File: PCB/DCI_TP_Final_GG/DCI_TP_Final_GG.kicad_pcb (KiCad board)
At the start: 2 copper layers, 42 x 90 mm, 69 parts, among them J201 DRIVER A OUT, J301 DRIVER B OUT, J401 IN - Driver A, J402 IN - Driver B, J403 Vin, J404 Vout, U201 A3967, U301 A3967, U401 LM317

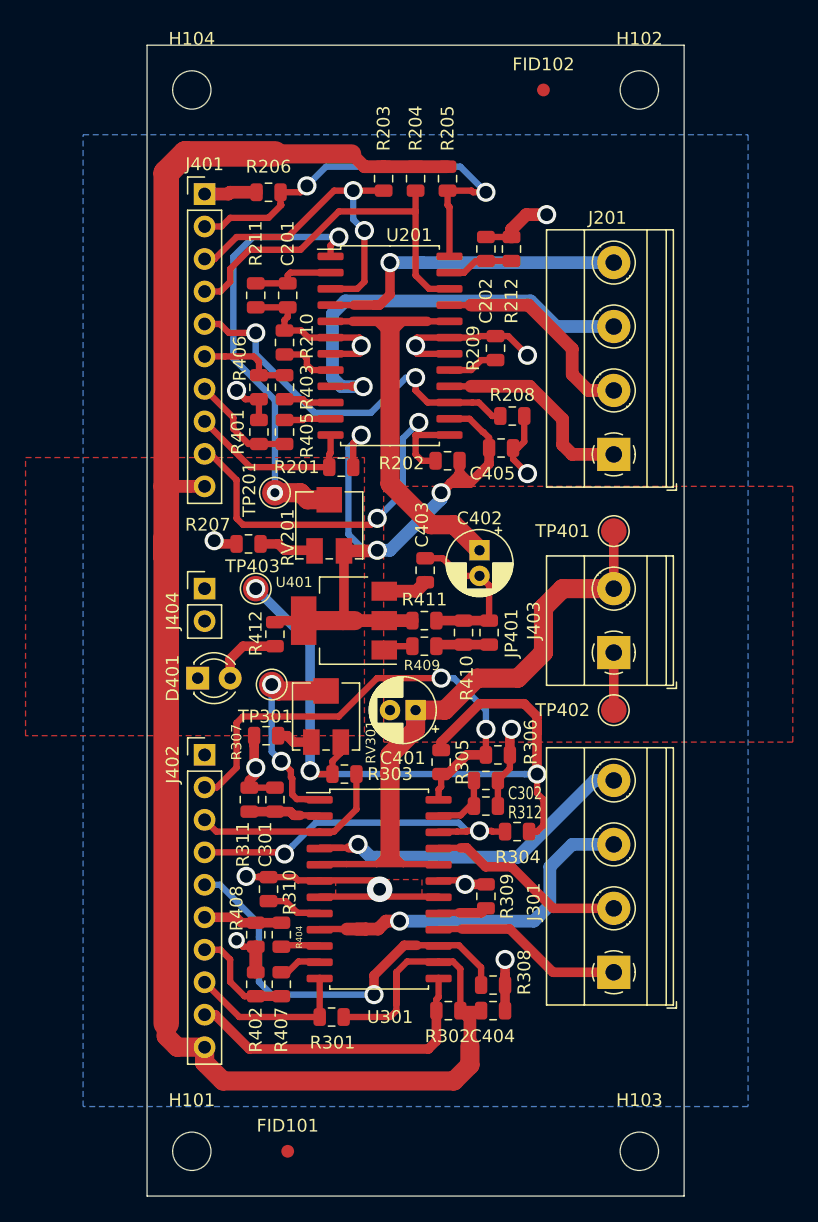
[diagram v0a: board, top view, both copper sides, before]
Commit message: Agrego 3D de borneras
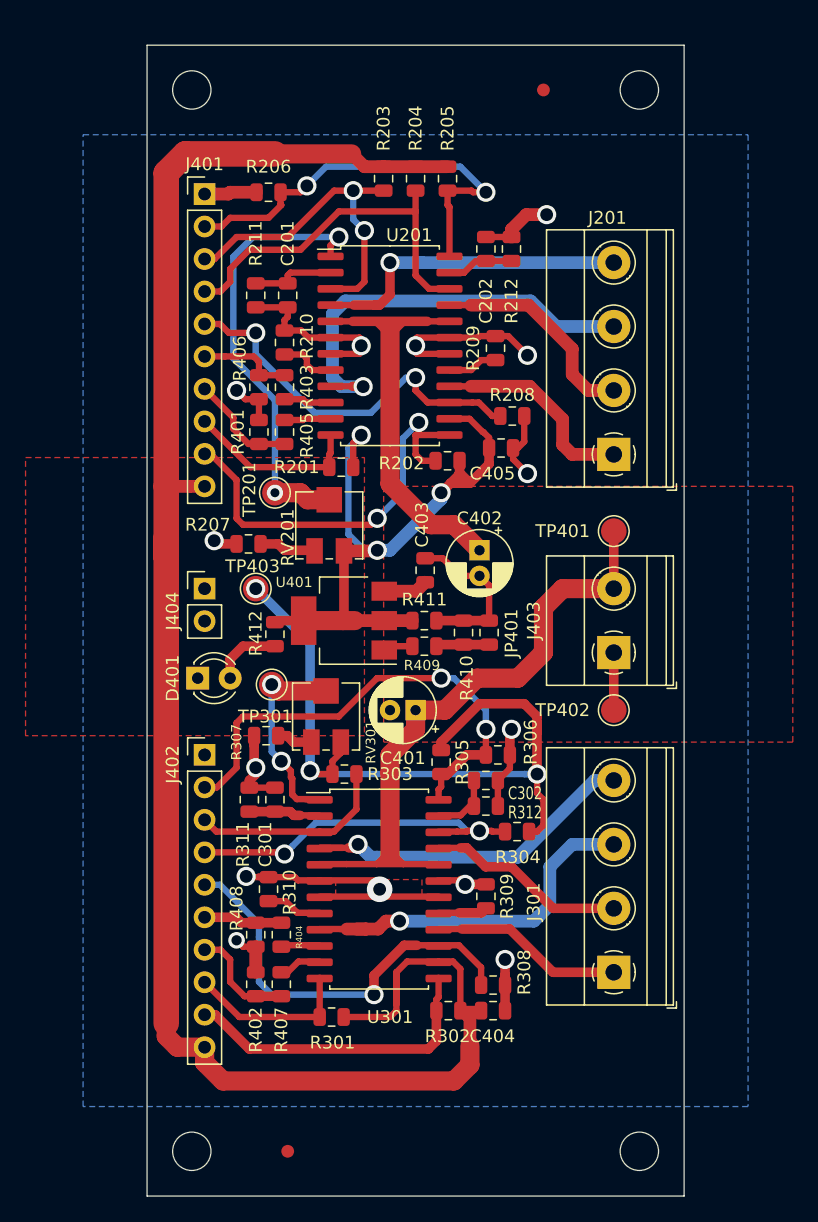
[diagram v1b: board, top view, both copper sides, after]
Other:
- board text added: "Grilla componentes: 5mm, 2,5mm, 1mm y 0.5mm(para ajuste fino en el control de clearance) Grilla pistas: 1mm, 0.5mm, 0.25mm y 0.1 (para ajuste fino) Vias: 1.3mm ,1.5mm y 2mm (Limite Mayer=1.27) Pistas: 0.5mm, 0.75mm, 1mm, 1.5mm, 2mm (limite Mayer = 0.3mm) Clearance > 0.3 mm (Limite Mayer=0.3mm) PCB FR4 - sustratos 1.6mm de espesor Cobre 1 Oz Terminacion HASL"
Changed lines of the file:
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@@
   (general
     (thickness 1.6)
-    (drawings 4)
+    (drawings 7)
     (tracks 558)
     (zones 0)
@@
     (0 F.Cu signal)
     (31 B.Cu signal)
-    (32 B.Adhes user hide)
-    (33 F.Adhes user hide)
-    (34 B.Paste user hide)
-    (35 F.Paste user hide)
+    (32 B.Adhes user)
+    (33 F.Adhes user)
+    (34 B.Paste user)
+    (35 F.Paste user)
     (36 B.SilkS user)
     (37 F.SilkS user)
     (38 B.Mask user)
     (39 F.Mask user)
-    (40 Dwgs.User user hide)
+    (40 Dwgs.User user)
     (41 Cmts.User user)
-    (42 Eco1.User user hide)
-    (43 Eco2.User user hide)
+    (42 Eco1.User user)
+    (43 Eco2.User user)
     (44 Edge.Cuts user)
     (45 Margin user)
-    (46 B.CrtYd user hide)
+    (46 B.CrtYd user)
     (47 F.CrtYd user)
-    (48 B.Fab user hide)
-    (49 F.Fab user hide)
+    (48 B.Fab user)
+    (49 F.Fab user)
   )
   (setup
-    (last_trace_width 0.75)
+    (last_trace_width 0.3)
     (user_trace_width 0.3)
     (user_trace_width 0.5)
@@
       (rotate (xyz 0 0 0))
     )
+    (model "${KIPRJMOD}/MKDS series connectors/3d_conn_mkds/walter/conn_mkds/mkds_1,5-4.wrl"
+      (offset (xyz 7.5 0 0))
+      (scale (xyz 1 1 1))
+      (rotate (xyz 0 0 0))
+    )
   )
   (module Package_SO:SOIC-24W_7.5x15.4mm_P1.27mm (layer F.Cu)
@@
       (net 1 GND))
     (model ${KISYS3DMOD}/TerminalBlock_Phoenix.3dshapes/TerminalBlock_Phoenix_MKDS-1,5-2_1x02_P5.00mm_Horizontal.wrl
-      (at (xyz 0 0 0))
+      (offset (xyz 0.5 0 0))
+      (scale (xyz 1 1 1))
+      (rotate (xyz 0 0 0))
+    )
+    (model "${KIPRJMOD}/MKDS series connectors/3d_conn_mkds/walter/conn_mkds/mkds_1,5-2.wrl"
+      (offset (xyz 2.5 0 0))
       (scale (xyz 1 1 1))
       (rotate (xyz 0 0 0))
@@
       (effects (font (size 1 1) (thickness 0.15)))
     )
-    (fp_text value "VRef A" (at 0 2.05 90) (layer F.Fab)
+    (fp_text value "VRef A" (at -0.5 2.25 90) (layer F.Fab)
       (effects (font (size 1 1) (thickness 0.15)))
     )
@@
       (effects (font (size 1 1) (thickness 0.15)))
     )
-    (fp_text value 1K (at 0 1.65 90) (layer F.Fab)
+    (fp_text value 1K (at 0 3.5 90) (layer F.Fab)
       (effects (font (size 1 1) (thickness 0.15)))
     )
@@
       (effects (font (size 1 1) (thickness 0.15)))
     )
-    (fp_text value 10K (at 0 1.65 90) (layer F.Fab)
+    (fp_text value 10K (at -0.0625 3.5 90) (layer F.Fab)
       (effects (font (size 1 1) (thickness 0.15)))
     )
@@
       (effects (font (size 1 1) (thickness 0.15)))
     )
-    (fp_text value 6.8K (at 0 1.65) (layer F.Fab)
+    (fp_text value 6.8K (at 1.5625 2.5) (layer F.Fab)
       (effects (font (size 1 1) (thickness 0.15)))
     )
@@
       (effects (font (size 1 1) (thickness 0.15)))
     )
-    (fp_text value Vout (at 0 4.87) (layer F.Fab)
+    (fp_text value Vout (at -2 2 90) (layer F.Fab)
       (effects (font (size 1 1) (thickness 0.15)))
     )
@@
       (net 12 "/Driver A/DA-O1A"))
     (model ${KISYS3DMOD}/TerminalBlock_Phoenix.3dshapes/TerminalBlock_Phoenix_MKDS-1,5-4_1x04_P5.00mm_Horizontal.wrl
-      (at (xyz 0 0 0))
+      (offset (xyz 0 -7.5 0))
+      (scale (xyz 1 1 1))
+      (rotate (xyz 0 0 0))
+    )
+    (model "${KIPRJMOD}/MKDS series connectors/3d_conn_mkds/walter/conn_mkds/mkds_1,5-4.wrl"
+      (offset (xyz 7.5 0 0))
       (scale (xyz 1 1 1))
       (rotate (xyz 0 0 0))
@@
     (tags "mounting hole 3mm no annular")
     (attr virtual)
-    (fp_text reference H104 (at 0 -4) (layer F.SilkS)
+    (fp_text reference H104 (at 0 4.5) (layer F.SilkS) hide
       (effects (font (size 1 1) (thickness 0.15)))
     )
@@
     (tags "mounting hole 3mm no annular")
     (attr virtual)
-    (fp_text reference H103 (at 0 -4) (layer F.SilkS)
+    (fp_text reference H103 (at 0 -4) (layer F.SilkS) hide
       (effects (font (size 1 1) (thickness 0.15)))
     )
@@
     (tags "mounting hole 3mm no annular")
     (attr virtual)
-    (fp_text reference H102 (at 0 -4) (layer F.SilkS)
+    (fp_text reference H102 (at 0 4.5) (layer F.SilkS) hide
       (effects (font (size 1 1) (thickness 0.15)))
     )
@@
     (tags "mounting hole 3mm no annular")
     (attr virtual)
-    (fp_text reference H101 (at 0 -4) (layer F.SilkS)
+    (fp_text reference H101 (at 0 -4) (layer F.SilkS) hide
       (effects (font (size 1 1) (thickness 0.15)))
     )
@@
     (tags fiducial)
     (attr smd)
-    (fp_text reference FID102 (at 0 -2) (layer F.SilkS)
+    (fp_text reference FID102 (at 0 -2) (layer F.SilkS) hide
       (effects (font (size 1 1) (thickness 0.15)))
     )
@@
     (tags fiducial)
     (attr smd)
-    (fp_text reference FID101 (at 0 -2) (layer F.SilkS)
+    (fp_text reference FID101 (at 0 -2) (layer F.SilkS) hide
       (effects (font (size 1 1) (thickness 0.15)))
     )
@@
       (effects (font (size 1 1) (thickness 0.15)))
     )
-    (fp_text value LED (at 1.27 2.96) (layer F.Fab)
+    (fp_text value LED (at -0.96 0.5 90) (layer F.Fab)
       (effects (font (size 1 1) (thickness 0.15)))
     )
@@
     )
   )
+  (dimension 90 (width 0.15) (layer F.Fab)
+    (gr_text "90,000 mm" (at 96.7 95.5 270) (layer F.Fab)
+      (effects (font (size 1 1) (thickness 0.15)))
+    )
+    (feature1 (pts (xy 106.5 140.5) (xy 97.413579 140.5)))
+    (feature2 (pts (xy 106.5 50.5) (xy 97.413579 50.5)))
+    (crossbar (pts (xy 98 50.5) (xy 98 140.5)))
+    (arrow1a (pts (xy 98 140.5) (xy 97.413579 139.373496)))
+    (arrow1b (pts (xy 98 140.5) (xy 98.586421 139.373496)))
+    (arrow2a (pts (xy 98 50.5) (xy 97.413579 51.626504)))
+    (arrow2b (pts (xy 98 50.5) (xy 98.586421 51.626504)))
+  )
+  (dimension 42 (width 0.15) (layer F.Fab)
+    (gr_text "42,000 mm" (at 127.5 43.2) (layer F.Fab)
+      (effects (font (size 1 1) (thickness 0.15)))
+    )
+    (feature1 (pts (xy 148.5 50.5) (xy 148.5 43.913579)))
+    (feature2 (pts (xy 106.5 50.5) (xy 106.5 43.913579)))
+    (crossbar (pts (xy 106.5 44.5) (xy 148.5 44.5)))
+    (arrow1a (pts (xy 148.5 44.5) (xy 147.373496 45.086421)))
+    (arrow1b (pts (xy 148.5 44.5) (xy 147.373496 43.913579)))
+    (arrow2a (pts (xy 106.5 44.5) (xy 107.626504 45.086421)))
+    (arrow2b (pts (xy 106.5 44.5) (xy 107.626504 43.913579)))
+  )
+  (gr_text "Grilla componentes: 5mm, 2,5mm,\n 1mm y 0.5mm(para ajuste fino en\nel control de clearance)\n\nGrilla pistas: 1mm, 0.5mm, 0.25mm \ny 0.1 (para ajuste fino)\n\nVias: 1.3mm ,1.5mm y 2mm (Limite Mayer=1.27)\n\nPistas: 0.5mm, 0.75mm, 1mm, 1.5mm, 2mm\n(limite Mayer = 0.3mm)\n\nClearance > 0.3 mm  (Limite Mayer=0.3mm)\n\nPCB\nFR4 - sustratos 1.6mm de espesor\nCobre 1 Oz\nTerminacion HASL\n\n" (at 175.5 87) (layer Dwgs.User)
+    (effects (font (size 1 1) (thickness 0.15)) (justify left))
+  )
   (gr_line (start 106.5 50.5) (end 106.5 140.5) (layer Edge.Cuts) (width 0.05))

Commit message: Agrego codigos de catalogo
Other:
- board text added: "Gonzalo Gontad DCI - CESE - FIUBA"
- board text added: "Industria Argentina"
- board text added: "V1019"
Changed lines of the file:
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@@
-(kicad_pcb (version 20171130) (host pcbnew "(5.1.4)-1")
+(kicad_pcb (version 20171130) (host pcbnew 5.1.4-e60b266~84~ubuntu18.04.1)
   (general
     (thickness 1.6)
-    (drawings 7)
+    (drawings 10)
     (tracks 558)
     (zones 0)
@@
   )
   (page A4)
+  (title_block
+    (title "Replica Dual EasyDriver v4.5")
+    (date 2019-10-17)
+    (rev "Matias Brignone")
+    (company "Gonzalo Gontad - CESE-FIUBA")
+  )
   (layers
     (0 F.Cu signal)
     (31 B.Cu signal)
-    (32 B.Adhes user)
-    (33 F.Adhes user)
-    (34 B.Paste user)
-    (35 F.Paste user)
-    (36 B.SilkS user)
+    (32 B.Adhes user hide)
+    (33 F.Adhes user hide)
+    (34 B.Paste user hide)
+    (35 F.Paste user hide)
+    (36 B.SilkS user hide)
     (37 F.SilkS user)
-    (38 B.Mask user)
+    (38 B.Mask user hide)
     (39 F.Mask user)
     (40 Dwgs.User user)
-    (41 Cmts.User user)
-    (42 Eco1.User user)
-    (43 Eco2.User user)
+    (41 Cmts.User user hide)
+    (42 Eco1.User user hide)
+    (43 Eco2.User user hide)
     (44 Edge.Cuts user)
     (45 Margin user)
-    (46 B.CrtYd user)
+    (46 B.CrtYd user hide)
     (47 F.CrtYd user)
-    (48 B.Fab user)
-    (49 F.Fab user)
+    (48 B.Fab user hide)
+    (49 F.Fab user hide)
   )
   (setup
@@
       (rotate (xyz 0 0 0))
     )
+    (model ${KIPRJMOD}/Potentiometer_SMD.3dshapes/Potentiometer_Bourns_3314J_Vertical.step
+      (at (xyz 0 0 0))
+      (scale (xyz 1 1 1))
+      (rotate (xyz 0 0 90))
+    )
   )
   (module Potentiometer_SMD:Potentiometer_Vishay_TS53YJ_Vertical (layer F.Cu)
@@
       (at (xyz 0 0 0))
       (scale (xyz 1 1 1))
-      (rotate (xyz 0 0 0))
+      (rotate (xyz 0 0 90))
+    )
+    (model ${KIPRJMOD}/Potentiometer_SMD.3dshapes/Potentiometer_Bourns_3314J_Vertical.step
+      (at (xyz 0 0 0))
+      (scale (xyz 1 1 1))
+      (rotate (xyz 0 0 90))
     )
   )
@@
     )
   )
+  (gr_text V1019 (at 130 135) (layer B.Cu)
+    (effects (font (size 1.5 1.5) (thickness 0.3)) (justify mirror))
+  )
+  (gr_text "Gonzalo Gontad\nDCI - CESE - FIUBA" (at 130 137.5) (layer F.SilkS)
+    (effects (font (size 1.3 1.3) (thickness 0.3)))
+  )
+  (gr_text "Industria Argentina" (at 125 52.5) (layer F.SilkS)
+    (effects (font (size 1.3 1.3) (thickness 0.3)))
+  )
   (dimension 90 (width 0.15) (layer F.Fab)
